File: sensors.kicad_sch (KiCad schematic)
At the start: 23 parts, among them U10 110-303, U5 BME688, U6 110-507, U7 MCP6042, U8 MCP6042, U9 ADS1015IDGS

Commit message: Finished schematic
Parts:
- removed U7, U8: MCP6042, Package_SO:SOIC-8_3.9x4.9mm_P1.27mm, symbol Device:Opamp_Dual
- added C9: 10uF, Capacitor_SMD:C_0805_2012Metric, symbol Device:C
- added D3: SMF5.0A, Diode_SMD:D_SOD-123, symbol Device:D_Zener
- added F1: 125mA, Fuse:Fuse_0603_1608Metric, symbol Device:Fuse
- added FB1: 600, Inductor_SMD:L_1206_3216Metric, symbol Device:FerriteBead
- added U10: INIR2-ME5, INIR2ME5, symbol INIR2-ME5:INIR2-ME5
- added U7, U8, U9: MCP6042, Package_SO:SOIC-8_3.9x4.9mm_P1.27mm, symbol Sensors:MCP6042
- C10: renamed from C8; footprint (none) -> Capacitor_SMD:C_0805_2012Metric; Manufacturer Part Number (none) -> C0805F104K1RACAUTO
- C11: renamed from C10; footprint (none) -> Capacitor_SMD:C_0805_2012Metric; Manufacturer Part Number (none) -> C0805F104K1RACAUTO
- C4: renamed from C5; footprint (none) -> Capacitor_SMD:C_0805_2012Metric; Manufacturer Part Number (none) -> CL21A106KOQNNNE
- C5: renamed from C3; value 100nF -> 0.1uF; footprint (none) -> Capacitor_SMD:C_0805_2012Metric; Manufacturer Part Number (none) -> C0805F104K1RACAUTO
- C6: renamed from C4; value 100nF -> 0.1uF; footprint (none) -> Capacitor_SMD:C_0805_2012Metric; Manufacturer Part Number (none) -> C0805F104K1RACAUTO
- C7: footprint (none) -> Capacitor_SMD:C_0805_2012Metric; Manufacturer Part Number (none) -> C0805F104K1RACAUTO
- C8: renamed from C9; footprint (none) -> Capacitor_SMD:C_0805_2012Metric; Manufacturer Part Number (none) -> C0805F104K1RACAUTO
- R11: renamed from R12; footprint (none) -> Resistor_SMD:R_0805_2012Metric; Manufacturer Part Number (none) -> RR1220P-103-D
- R12: renamed from R11; footprint (none) -> Resistor_SMD:R_0805_2012Metric; Manufacturer Part Number (none) -> RR1220P-103-D
- R13: renamed from R17; footprint (none) -> Resistor_SMD:R_0603_1608Metric; Manufacturer Part Number (none) -> ERA-3AEB151V
- R14: renamed from R19; footprint (none) -> Resistor_SMD:R_0603_1608Metric; Manufacturer Part Number (none) -> ERA-3AEB151V
- R15: renamed from R13; value 103k -> 102k; footprint (none) -> Resistor_SMD:R_0603_1608Metric; Manufacturer Part Number (none) -> RC0603FR-07102KL
- R16: renamed from R14; footprint (none) -> Resistor_SMD:R_0603_1608Metric; Manufacturer Part Number (none) -> RC0603FR-07100KL
- R17: renamed from R15; footprint (none) -> Resistor_SMD:R_0603_1608Metric; Manufacturer Part Number (none) -> RC0603FR-07100KL
- R18: renamed from R16; footprint (none) -> Resistor_SMD:R_0603_1608Metric; Manufacturer Part Number (none) -> RC0603FR-07100KL
- R19: renamed from R18; value R -> 6.8M; footprint (none) -> Resistor_SMD:R_0603_1608Metric; Manufacturer Part Number (none) -> RC0603JR-076M8L
- R20: renamed from R22; value R -> 100k; footprint (none) -> Resistor_SMD:R_0603_1608Metric; Manufacturer Part Number (none) -> RC0603FR-07100KL
- U5: renamed from U9; Manufacturer Part Number (none) -> ADS1015IDGSR
- U6: renamed from U5; Manufacturer Part Number (none) -> BME688
- renumbered U6 to U11, U10 to U12
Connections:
- net +3.3V: now also C9.1, FB1.2, U7.4 (V-), U8.4 (V-), U9.4 (V-)
- net GND: now also C9.2, D3.2 (A), U10.3 (GND), U7.8 (V+), U8.8 (V+), U9.8 (V+)
- net VCH4: now also U7.1, U7.2 (-)
- net VH2S: now also U9.7
- net VNO2: now also U8.7
- net Vref: now also U8.3 (+), U9.3 (+), U9.5 (+)
- net at C10.1, R13.2, R19.1: now also U8.6 (-)
- net at C7.2, U11.5 (Counter): now also U8.1
- net at C7.1, U11.4 (Reference): now also U8.2 (-)
- net at R15.1, R16.2: now also U8.5 (+)
- net at C8.2, U12.5 (Counter): now also U9.1
- net at C8.1, U12.4 (Reference): now also U9.2 (-)
- net at C11.1, R14.2, R20.1: now also U9.6 (-)
- new net: U10.5 (OUT), U7.3 (+)
- new net: F1.1, U10.2 (VIN)
- new net: D3.1 (K), F1.2, FB1.1
- new net Sensor_RX: U10.4 (RXD)
- new net Sensor_TX: U10.1 (TXD)
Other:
- note added: "CH4"
- note added: "VOCs"
- note removed: "TODO pick this"
- moved on the sheet: R17, R18

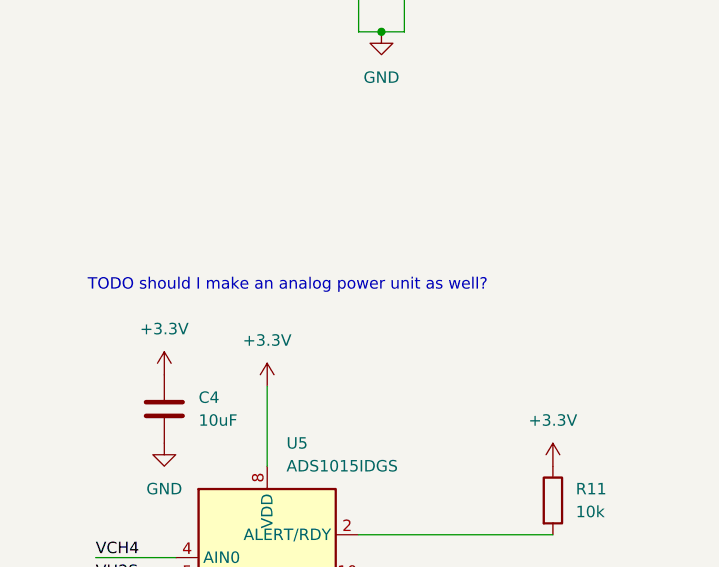
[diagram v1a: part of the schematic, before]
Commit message: Finished first footprint (no routing)
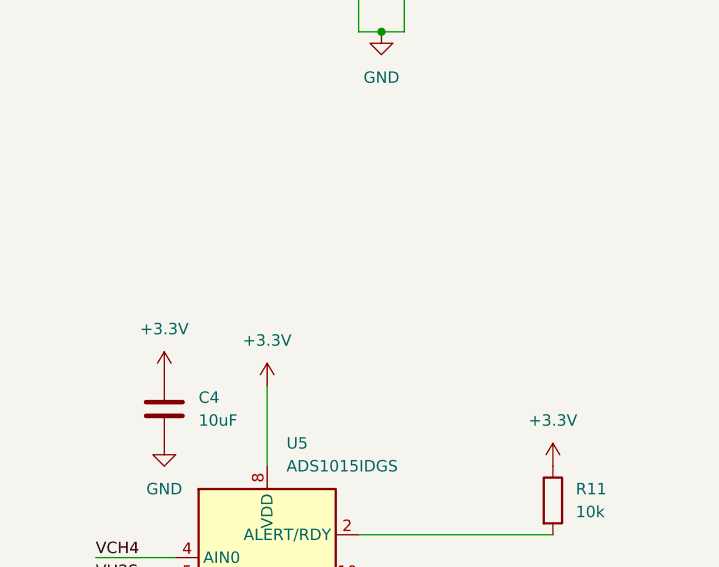
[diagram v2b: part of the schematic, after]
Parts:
- C4, C9: footprint Capacitor_SMD:C_0805_2012Metric -> Capacitor_SMD:C_1206_3216Metric; Manufacturer Part Number CL21A106KOQNNNE -> TMK316BJ106KL-T
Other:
- note removed: "TODO should I make an analog power unit as well?"
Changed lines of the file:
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@@
 		(comment 2 "Designed by")
 	)
-	(text "TODO should I make an analog power unit as well?"
-		(exclude_from_sim no)
-		(at 44.196 108.204 0)
-		(effects
-			(font
-				(size 1.27 1.27)
-			)
-		)
-	)
 	(text "NO2"
 		(exclude_from_sim no)
@@
 		)
 		(instances
-			(project ""
+			(project "AirQualityPCB"
 				(path "/91f71406-0d85-449c-a1a7-616be8373eb5/7e08e9d5-6e56-40af-b2c7-a3b6d3605d5b"
 					(reference "U9")
@@
 			)
 		)
-		(property "Footprint" "Capacitor_SMD:C_0805_2012Metric"
+		(property "Footprint" "Capacitor_SMD:C_1206_3216Metric"
 			(at 31.4452 125.73 0)
 			(effects
@@
 			)
 		)
-		(property "Manufacturer Part Number" "CL21A106KOQNNNE"
+		(property "Manufacturer Part Number" "TMK316BJ106KL-T"
 			(at 30.48 121.92 0)
 			(effects
@@
 				)
 			)
-			(project ""
+			(project "AirQualityPCB"
 				(path "/91f71406-0d85-449c-a1a7-616be8373eb5/7e08e9d5-6e56-40af-b2c7-a3b6d3605d5b"
 					(reference "C4")
@@
 			)
 		)
-		(property "Footprint" "Capacitor_SMD:C_0805_2012Metric"
+		(property "Footprint" "Capacitor_SMD:C_1206_3216Metric"
 			(at 194.0052 157.48 0)
 			(effects
@@
 			)
 		)
-		(property "Manufacturer Part Number" "CL21A106KOQNNNE"
+		(property "Manufacturer Part Number" "TMK316BJ106KL-T"
 			(at 193.04 153.67 0)
 			(effects
@@
 		)
 		(instances
-			(project ""
+			(project "AirQualityPCB"
 				(path "/91f71406-0d85-449c-a1a7-616be8373eb5/7e08e9d5-6e56-40af-b2c7-a3b6d3605d5b"
 					(reference "C9")
@@
 		)
 		(instances
-			(project ""
+			(project "AirQualityPCB"
 				(path "/91f71406-0d85-449c-a1a7-616be8373eb5/7e08e9d5-6e56-40af-b2c7-a3b6d3605d5b"
 					(reference "U7")
@@
 				)
 			)
-			(project ""
+			(project "AirQualityPCB"
 				(path "/91f71406-0d85-449c-a1a7-616be8373eb5/7e08e9d5-6e56-40af-b2c7-a3b6d3605d5b"
 					(reference "R13")
@@
 				)
 			)
-			(project ""
+			(project "AirQualityPCB"
 				(path "/91f71406-0d85-449c-a1a7-616be8373eb5/7e08e9d5-6e56-40af-b2c7-a3b6d3605d5b"
 					(reference "U5")
@@
 				)
 			)
-			(project ""
+			(project "AirQualityPCB"
 				(path "/91f71406-0d85-449c-a1a7-616be8373eb5/7e08e9d5-6e56-40af-b2c7-a3b6d3605d5b"
 					(reference "C7")
@@
 		)
 		(instances
-			(project ""
+			(project "AirQualityPCB"
 				(path "/91f71406-0d85-449c-a1a7-616be8373eb5/7e08e9d5-6e56-40af-b2c7-a3b6d3605d5b"
 					(reference "U9")
@@
 				)
 			)
-			(project ""
+			(project "AirQualityPCB"
 				(path "/91f71406-0d85-449c-a1a7-616be8373eb5/7e08e9d5-6e56-40af-b2c7-a3b6d3605d5b"
 					(reference "#PWR031")
@@
 		)
 		(instances
-			(project ""
+			(project "AirQualityPCB"
 				(path "/91f71406-0d85-449c-a1a7-616be8373eb5/7e08e9d5-6e56-40af-b2c7-a3b6d3605d5b"
 					(reference "U7")
@@
 				)
 			)
-			(project ""
+			(project "AirQualityPCB"
 				(path "/91f71406-0d85-449c-a1a7-616be8373eb5/7e08e9d5-6e56-40af-b2c7-a3b6d3605d5b"
 					(reference "C5")
@@
 		)
 		(instances
-			(project ""
+			(project "AirQualityPCB"
 				(path "/91f71406-0d85-449c-a1a7-616be8373eb5/7e08e9d5-6e56-40af-b2c7-a3b6d3605d5b"
 					(reference "U8")
@@
 				)
 			)
-			(project ""
+			(project "AirQualityPCB"
 				(path "/91f71406-0d85-449c-a1a7-616be8373eb5/7e08e9d5-6e56-40af-b2c7-a3b6d3605d5b"
 					(reference "U6")
@@
 		)
 		(instances
-			(project ""
+			(project "AirQualityPCB"
 				(path "/91f71406-0d85-449c-a1a7-616be8373eb5/7e08e9d5-6e56-40af-b2c7-a3b6d3605d5b"
 					(reference "U8")
@@
 				)
 			)
-			(project ""
+			(project "AirQualityPCB"
 				(path "/91f71406-0d85-449c-a1a7-616be8373eb5/7e08e9d5-6e56-40af-b2c7-a3b6d3605d5b"
 					(reference "#PWR029")
@@
 		)
 		(instances
-			(project ""
+			(project "AirQualityPCB"
 				(path "/91f71406-0d85-449c-a1a7-616be8373eb5/7e08e9d5-6e56-40af-b2c7-a3b6d3605d5b"
 					(reference "D3")
@@
 		)
 		(instances
-			(project ""
+			(project "AirQualityPCB"
 				(path "/91f71406-0d85-449c-a1a7-616be8373eb5/7e08e9d5-6e56-40af-b2c7-a3b6d3605d5b"
 					(reference "U8")
@@
 				)
 			)
-			(project ""
+			(project "AirQualityPCB"
 				(path "/91f71406-0d85-449c-a1a7-616be8373eb5/7e08e9d5-6e56-40af-b2c7-a3b6d3605d5b"
 					(reference "U12")
@@
 				)
 			)
-			(project ""
+			(project "AirQualityPCB"
 				(path "/91f71406-0d85-449c-a1a7-616be8373eb5/7e08e9d5-6e56-40af-b2c7-a3b6d3605d5b"
 					(reference "R12")
@@
 		)
 		(instances
-			(project ""
+			(project "AirQualityPCB"
 				(path "/91f71406-0d85-449c-a1a7-616be8373eb5/7e08e9d5-6e56-40af-b2c7-a3b6d3605d5b"
 					(reference "U9")
@@
 				)
 			)
-			(project ""
+			(project "AirQualityPCB"
 				(path "/91f71406-0d85-449c-a1a7-616be8373eb5/7e08e9d5-6e56-40af-b2c7-a3b6d3605d5b"
 					(reference "U11")

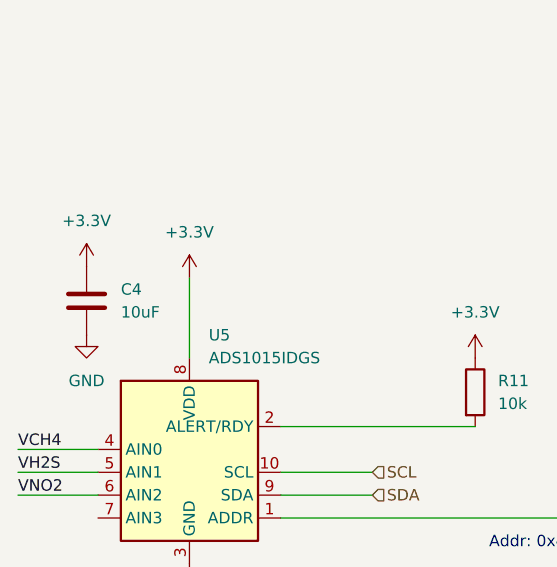
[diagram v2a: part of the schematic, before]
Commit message: Removed components pre quilter routing
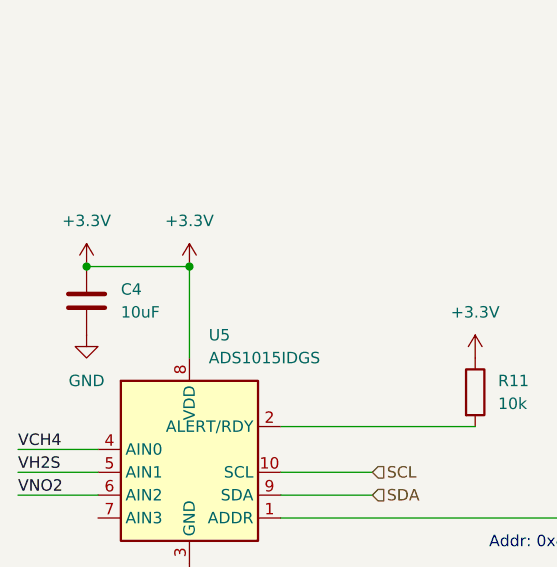
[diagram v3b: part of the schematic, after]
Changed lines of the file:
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@@
+	)
+	(junction
+		(at 30.48 118.11)
+		(diameter 0)
+		(color 0 0 0 0)
 	)
 	(junction
@@
 	)
 	(junction
+		(at 41.91 118.11)
+		(diameter 0)
+		(color 0 0 0 0)
+	)
+	(junction
 		(at 147.32 90.17)
 		(diameter 0)
@@
 	(wire
 		(pts
+			(xy 30.48 118.11) (xy 41.91 118.11)
+		)
+		(stroke
+			(width 0)
+			(type default)
+		)
+	)
+	(wire
+		(pts
 			(xy 147.32 27.94) (xy 157.48 27.94)
 		)
@@
 	(wire
 		(pts
-			(xy 41.91 119.38) (xy 41.91 128.27)
+			(xy 41.91 118.11) (xy 41.91 128.27)
 		)
 		(stroke
@@
 	(symbol
 		(lib_id "power:+3.3V")
-		(at 41.91 119.38 0)
+		(at 41.91 118.11 0)
 		(unit 1)
 		(exclude_from_sim no)
@@
 		(fields_autoplaced yes)
 		(property "Reference" "#PWR028"
-			(at 41.91 123.19 0)
+			(at 41.91 121.92 0)
 			(effects
 				(font
@@
 		)
 		(property "Value" "+3.3V"
-			(at 41.91 114.3 0)
+			(at 41.91 113.03 0)
 			(effects
 				(font
@@
 		)
 		(property "Footprint" ""
-			(at 41.91 119.38 0)
+			(at 41.91 118.11 0)
 			(effects
 				(font
@@
 		)
 		(property "Datasheet" ""
-			(at 41.91 119.38 0)
+			(at 41.91 118.11 0)
 			(effects
 				(font
@@
 		)
 		(property "Description" "Power symbol creates a global label with name \"+3.3V\""
-			(at 41.91 119.38 0)
-			(effects
-				(font
+			(at 41.91 118.11 0)
+			(effects
+				(font
